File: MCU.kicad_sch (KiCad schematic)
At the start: 17 parts, among them J3 ICSP, J4 PROG, SW1 RESET, U1 CSTCE16M0V53-R0, U2 ATmega2560-16A

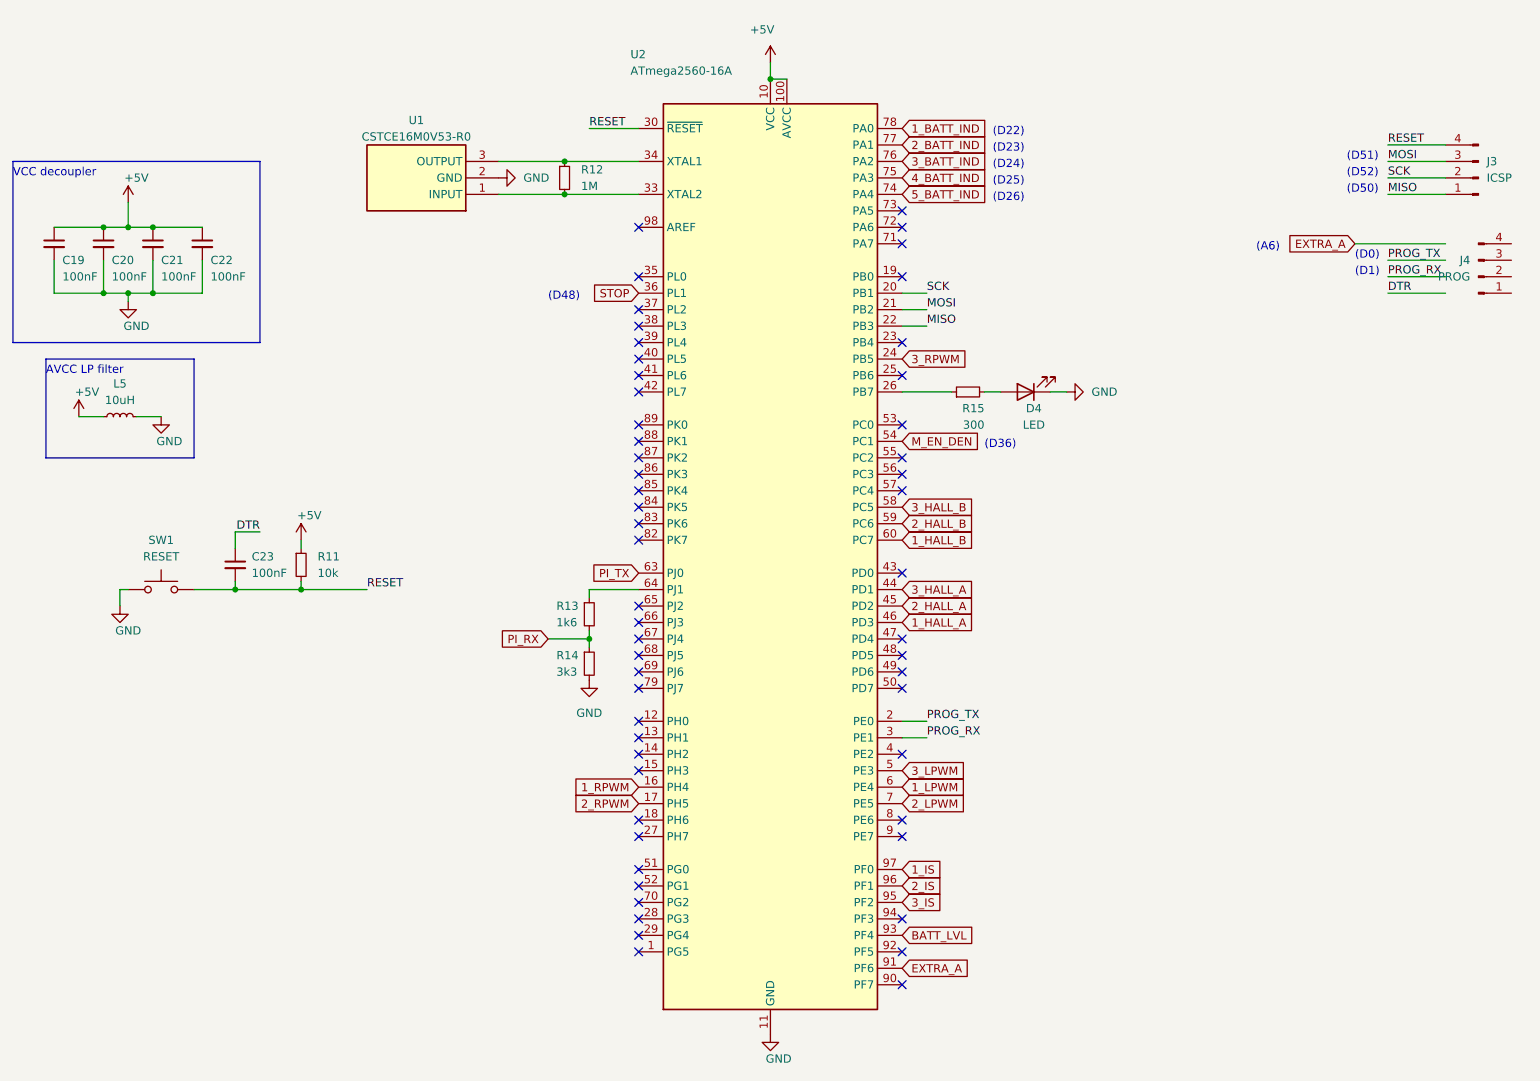
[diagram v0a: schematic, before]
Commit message: MCU routing completed
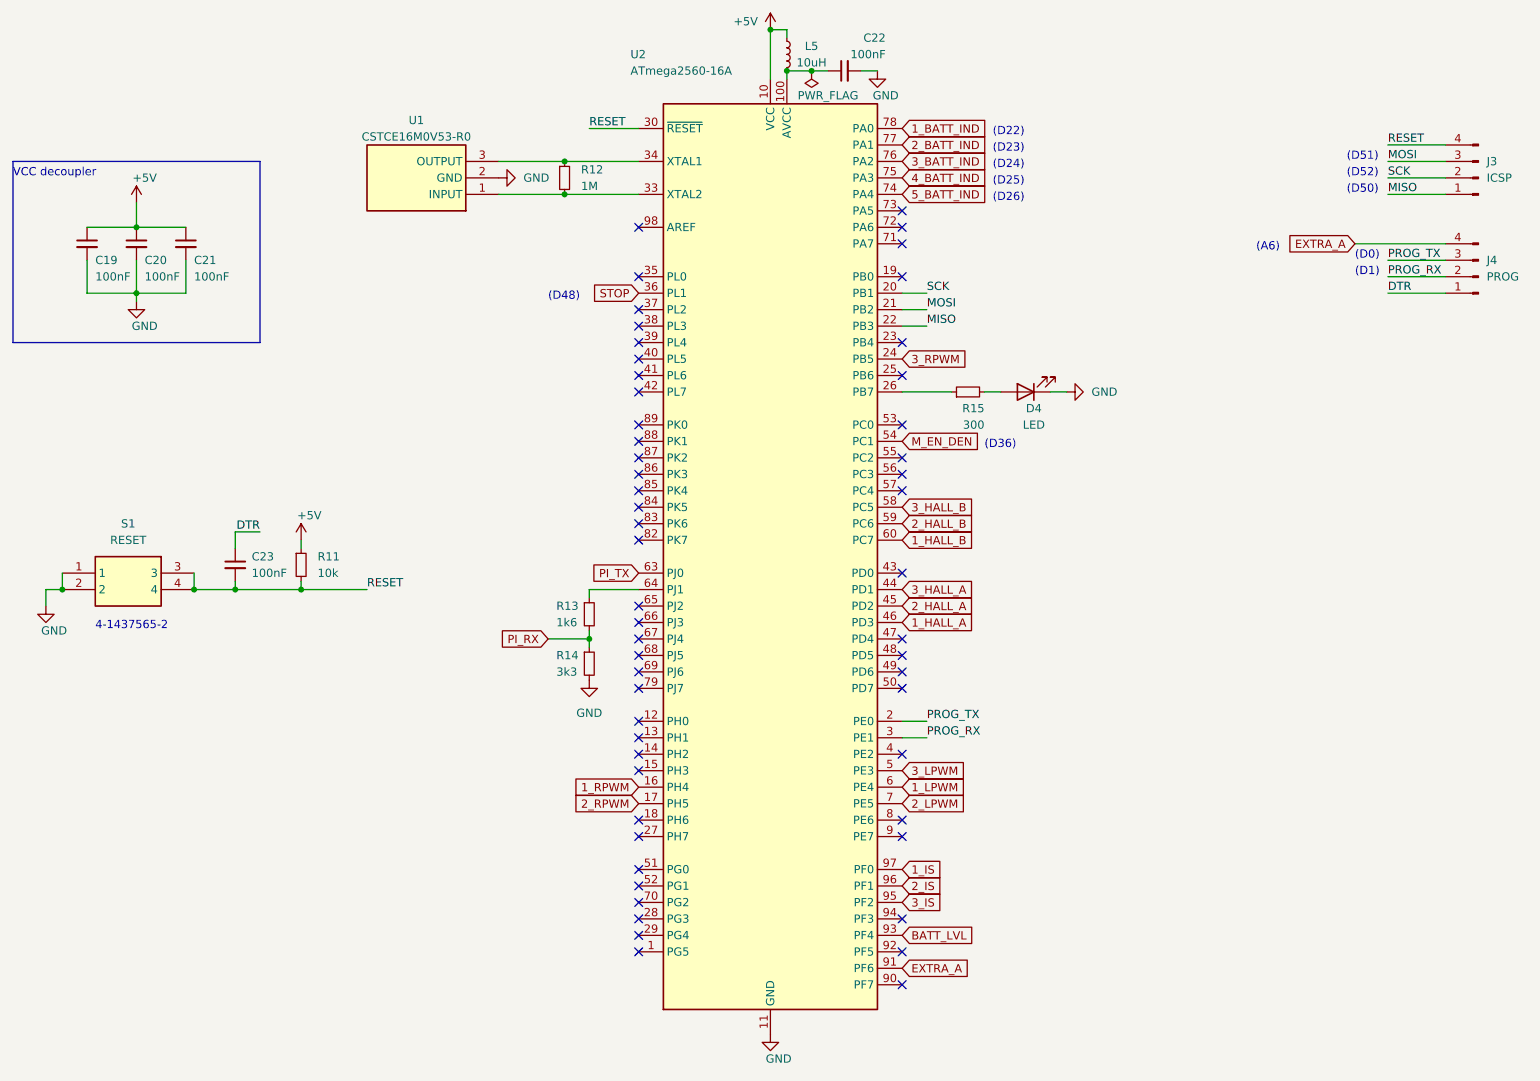
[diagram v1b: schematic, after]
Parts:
- removed SW1: RESET, Connector_PinHeader_2.54mm:PinHeader_1x02_P2.54mm_Vertical, symbol Switch:SW_Push
- added S1: RESET, SamacSys_Parts:FSM4JSMATR, symbol SamacSys_Parts:FSM4JSMATR
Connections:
- net +5V: no longer C22.1, U2.100 (AVCC)
- net DTR: now also J4.1 (Pin_1)
- net EXTRA_A: now also J4.4 (Pin_4)
- net GND: now also S1.1, S1.2; no longer L5.2
- net PROG_RX: now also J4.2 (Pin_2)
- net PROG_TX: now also J4.3 (Pin_3)
- net RESET: now also S1.3, S1.4
- new net: C22.1, L5.2, U2.100 (AVCC)
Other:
- note added: "4-1437565-2"
- note removed: "AVCC LP filter"
- moved on the sheet: C19, C20, C21, J4, L5
